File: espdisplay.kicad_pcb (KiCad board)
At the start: 2 copper layers, 34.3 x 30 mm, 11 parts, among them J1 PWR, J2 UReg, J3 DOut, J4 Serial, J5 IO32, SW1 RESET, SW2 BOOT, U1 ESP-WROOM-32

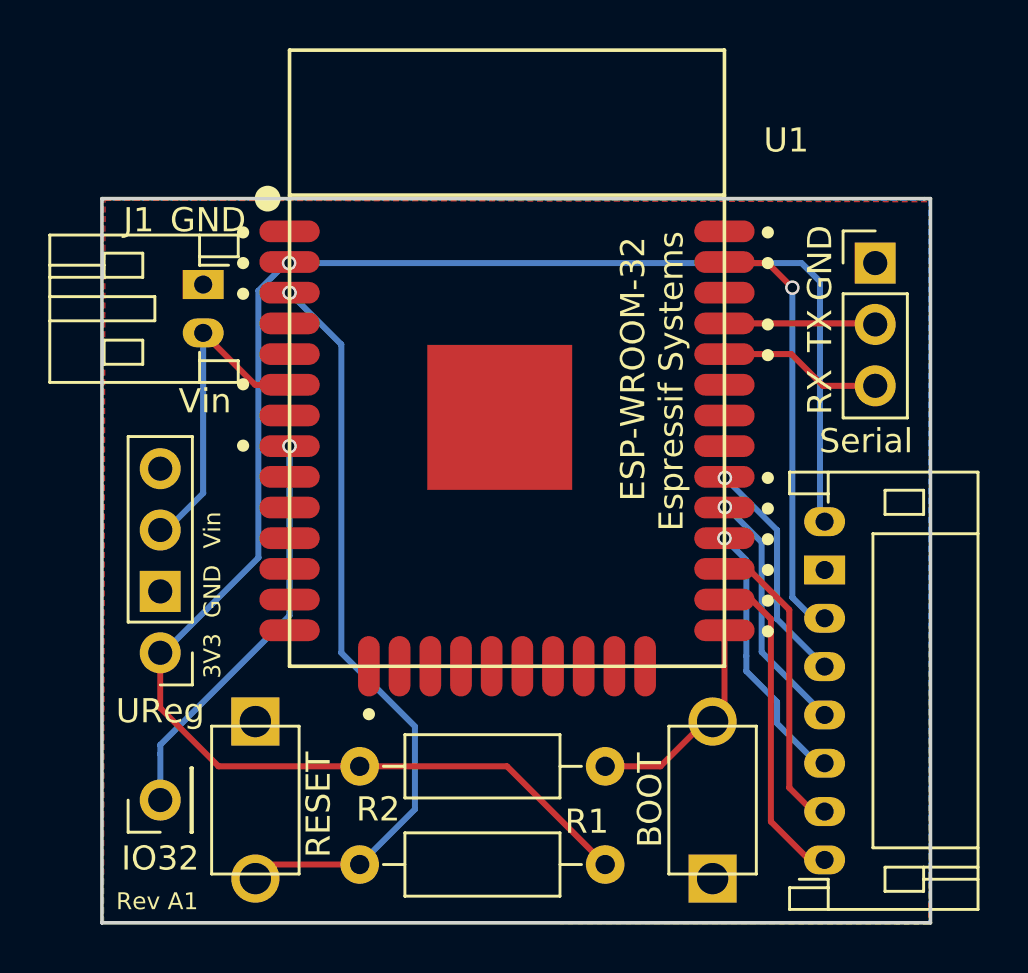
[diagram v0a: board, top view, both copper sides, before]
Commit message: Vias 0.65mm
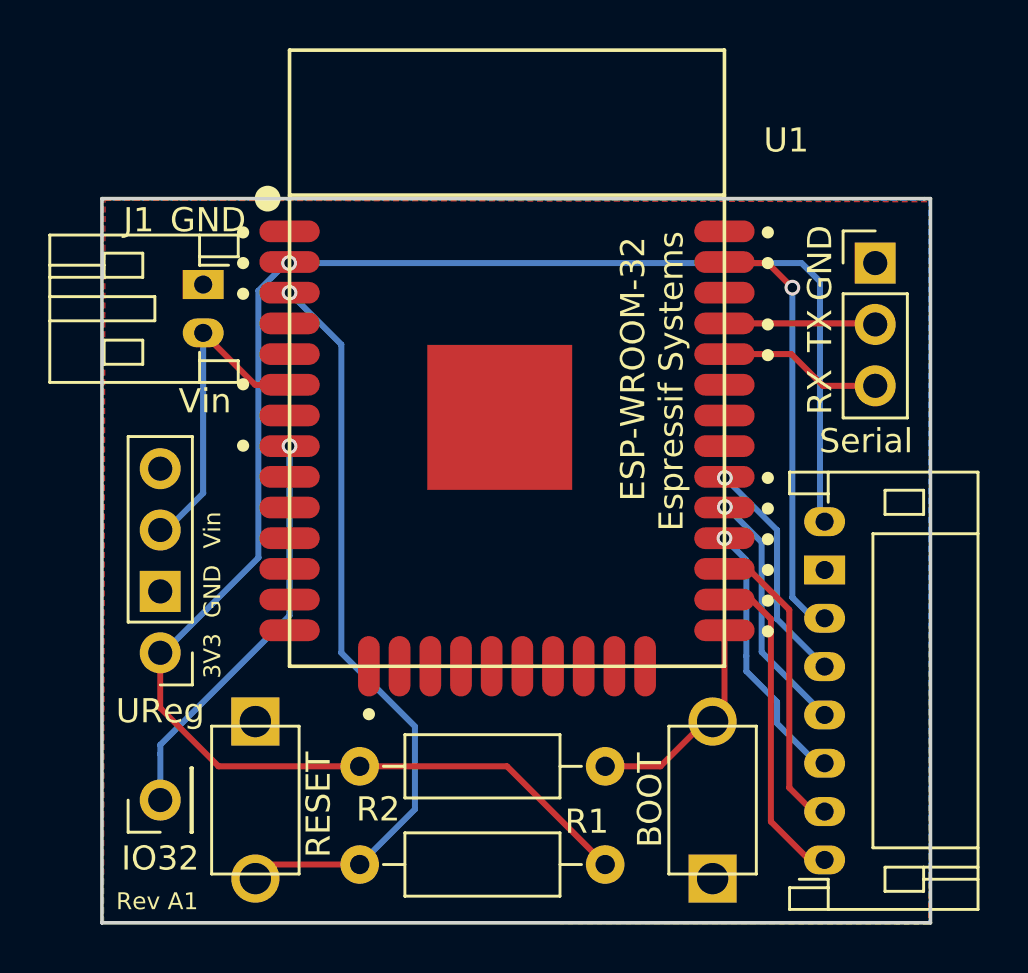
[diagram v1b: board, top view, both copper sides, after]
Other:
- net class Default: via_dia 0.6 -> 0.65
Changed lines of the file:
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@@
     (segment_width 0.25)
     (edge_width 0.15)
-    (via_size 0.6)
+    (via_size 0.65)
     (via_drill 0.4)
     (via_min_size 0.6)
@@
     (clearance 0.2)
     (trace_width 0.25)
-    (via_dia 0.6)
+    (via_dia 0.65)
     (via_drill 0.4)
     (uvia_dia 0.3)
@@
   (segment (start 177.3465 105.263) (end 177.537 105.4535) (width 0.25) (layer B.Cu) (net 3) (status 30))
   (segment (start 155.3755 94.752) (end 155.3925 94.735) (width 0.25) (layer F.Cu) (net 3) (status 30))
-  (via (at 155.3755 94.752) (size 0.6) (drill 0.4) (layers F.Cu B.Cu) (net 3) (status 30))
+  (via (at 155.3755 94.752) (size 0.65) (drill 0.4) (layers F.Cu B.Cu) (net 3) (status 30))
   (segment (start 155.3925 94.735) (end 155.3925 94.709) (width 0.25) (layer F.Cu) (net 3) (status 30))
   (segment (start 155.5025 94.625) (end 155.3925 94.709) (width 0.25) (layer F.Cu) (net 3) (status 80030))
@@
   (segment (start 175.1875 94.752) (end 173.4355 94.752) (width 0.25) (layer F.Cu) (net 4))
   (segment (start 177.062 109.4535) (end 176.2035 108.595) (width 0.25) (layer B.Cu) (net 4))
-  (via (at 176.2035 95.768) (size 0.6) (drill 0.4) (layers F.Cu B.Cu) (net 4))
+  (via (at 176.2035 95.768) (size 0.65) (drill 0.4) (layers F.Cu B.Cu) (net 4))
   (segment (start 176.2035 108.595) (end 176.2035 95.768) (width 0.25) (layer B.Cu) (net 4))
   (segment (start 177.537 109.4535) (end 177.062 109.4535) (width 0.25) (layer B.Cu) (net 4))
   (segment (start 173.3925 103.599) (end 173.3925 103.625) (width 0.25) (layer F.Cu) (net 5) (status 30))
   (segment (start 173.3925 103.625) (end 173.4095 103.642) (width 0.25) (layer F.Cu) (net 5) (status 30))
-  (via (at 173.4095 103.642) (size 0.6) (drill 0.4) (layers F.Cu B.Cu) (net 5) (status 30))
+  (via (at 173.4095 103.642) (size 0.65) (drill 0.4) (layers F.Cu B.Cu) (net 5) (status 30))
   (segment (start 173.4095 103.642) (end 175.5685 105.801) (width 0.25) (layer B.Cu) (net 5))
   (segment (start 175.5685 105.801) (end 175.5685 109.485) (width 0.25) (layer B.Cu) (net 5))
@@
   (segment (start 174.9335 106.309) (end 174.9335 110.85) (width 0.25) (layer B.Cu) (net 6))
   (segment (start 173.3925 104.8655) (end 173.4095 104.8485) (width 0.25) (layer F.Cu) (net 6) (status 30))
-  (via (at 173.4095 104.8485) (size 0.6) (drill 0.4) (layers F.Cu B.Cu) (net 6) (status 30))
+  (via (at 173.4095 104.8485) (size 0.65) (drill 0.4) (layers F.Cu B.Cu) (net 6) (status 30))
   (segment (start 173.3925 104.869) (end 173.3925 104.8655) (width 0.25) (layer F.Cu) (net 6) (status 30))
   (segment (start 177.537 115.4535) (end 177.22 115.4535) (width 0.25) (layer B.Cu) (net 7))
@@
   (segment (start 174.2985 111.643) (end 175.5685 112.913) (width 0.25) (layer B.Cu) (net 7))
   (segment (start 174.2985 111.008) (end 174.2985 111.643) (width 0.25) (layer B.Cu) (net 7))
-  (via (at 173.3925 106.139) (size 0.6) (drill 0.4) (layers F.Cu B.Cu) (net 7))
+  (via (at 173.3925 106.139) (size 0.65) (drill 0.4) (layers F.Cu B.Cu) (net 7))
   (segment (start 174.2985 107.045) (end 174.2985 111.008) (width 0.25) (layer B.Cu) (net 7))
   (segment (start 174.2985 107.045) (end 173.3925 106.139) (width 0.25) (layer B.Cu) (net 7))
@@
   (segment (start 160.5825 117.358) (end 158.2965 119.644) (width 0.25) (layer B.Cu) (net 10) (status 20))
   (segment (start 160.5825 113.929) (end 160.5825 117.358) (width 0.25) (layer B.Cu) (net 10))
-  (via (at 155.3925 95.979) (size 0.6) (drill 0.4) (layers F.Cu B.Cu) (net 10) (status 30))
+  (via (at 155.3925 95.979) (size 0.65) (drill 0.4) (layers F.Cu B.Cu) (net 10) (status 30))
   (segment (start 155.3925 95.979) (end 157.5345 98.121) (width 0.25) (layer B.Cu) (net 10))
   (segment (start 157.5345 98.121) (end 157.5345 110.881) (width 0.25) (layer B.Cu) (net 10))
@@
   (segment (start 150.0415 114.691) (end 150.0415 115.072) (width 0.25) (layer B.Cu) (net 37))
   (segment (start 150.0415 115.072) (end 150.0415 116.977) (width 0.25) (layer B.Cu) (net 37))
-  (via (at 155.3925 102.329) (size 0.6) (drill 0.4) (layers F.Cu B.Cu) (net 37))
+  (via (at 155.3925 102.329) (size 0.65) (drill 0.4) (layers F.Cu B.Cu) (net 37))
   (zone (net 2) (net_name GND) (layer F.Cu) (hatch edge 0.508)
     (connect_pads (clearance 0.508))

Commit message: Trace width
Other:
- net class PWR added: clearance 0.2, trace_width 0.6, via_dia 0.8, via_drill 0.4
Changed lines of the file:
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@@
     (links 28)
     (no_connects 0)
-    (area 143.5945 83.49 185.862 122.132001)
+    (area 147.553499 92.009999 181.993501 122.132001)
     (thickness 1.6)
     (drawings 38)
-    (tracks 89)
+    (tracks 79)
     (zones 0)
     (modules 11)
@@
     (uvia_dia 0.3)
     (uvia_drill 0.1)
-    (add_net +3V3)
     (add_net /BUSY)
     (add_net /CLK)
@@
     (add_net /IO32)
     (add_net /RST)
-    (add_net /Vin)
-    (add_net GND)
     (add_net "Net-(J2-Pad4)")
     (add_net "Net-(J4-Pad2)")
@@
     (add_net "Net-(U1-Pad7)")
     (add_net "Net-(U1-Pad9)")
+  )
+  (net_class PWR ""
+    (clearance 0.2)
+    (trace_width 0.6)
+    (via_dia 0.8)
+    (via_drill 0.4)
+    (uvia_dia 0.3)
+    (uvia_drill 0.1)
+    (add_net +3V3)
+    (add_net /Vin)
+    (add_net GND)
   )
   (module Symbols:OSHW-Logo_7.5x8mm_SilkScreen (layer B.Cu)
@@
   )
   (segment (start 150.0415 105.801) (end 150.2955 105.801) (width 0.25) (layer B.Cu) (net 1))
-  (segment (start 150.2955 105.801) (end 151.8195 104.277) (width 0.25) (layer B.Cu) (net 1))
-  (segment (start 151.8195 97.641) (end 151.8195 104.277) (width 0.25) (layer B.Cu) (net 1) (status 10))
-  (segment (start 155.3925 99.789) (end 153.9675 99.789) (width 0.25) (layer F.Cu) (net 1) (status 10))
-  (segment (start 153.9675 99.789) (end 151.8195 97.641) (width 0.25) (layer F.Cu) (net 1) (status 20))
-  (segment (start 155.3755 94.752) (end 155.2485 94.752) (width 0.25) (layer B.Cu) (net 3))
-  (segment (start 155.2485 94.752) (end 154.1055 95.895) (width 0.25) (layer B.Cu) (net 3))
+  (segment (start 150.2955 105.801) (end 151.8195 104.277) (width 0.6) (layer B.Cu) (net 1))
+  (segment (start 151.8195 97.641) (end 151.8195 104.277) (width 0.6) (layer B.Cu) (net 1) (status 10))
+  (segment (start 155.3925 99.789) (end 153.9675 99.789) (width 0.6) (layer F.Cu) (net 1) (status 10))
+  (segment (start 153.9675 99.789) (end 151.8195 97.641) (width 0.6) (layer F.Cu) (net 1) (status 20))
+  (segment (start 155.3755 94.752) (end 154.294924 95.832576) (width 0.6) (layer B.Cu) (net 3))
+  (segment (start 154.294924 95.832576) (end 154.294924 106.754576) (width 0.6) (layer B.Cu) (net 3))
+  (segment (start 154.294924 106.754576) (end 150.1685 110.881) (width 0.6) (layer B.Cu) (net 3))
   (segment (start 150.0415 110.881) (end 150.1685 110.881) (width 0.25) (layer B.Cu) (net 3))
-  (segment (start 150.1685 110.881) (end 154.1055 106.944) (width 0.25) (layer B.Cu) (net 3))
-  (segment (start 154.1055 95.895) (end 154.1055 106.944) (width 0.25) (layer B.Cu) (net 3))
-  (segment (start 177.3465 95.514) (end 176.5845 94.752) (width 0.25) (layer B.Cu) (net 3))
-  (segment (start 177.3465 95.514) (end 177.3465 105.263) (width 0.25) (layer B.Cu) (net 3))
-  (segment (start 158.2965 115.58) (end 152.4545 115.58) (width 0.25) (layer F.Cu) (net 3) (status 10))
-  (segment (start 150.0415 113.167) (end 150.0415 110.881) (width 0.25) (layer F.Cu) (net 3))
-  (segment (start 152.4545 115.58) (end 150.0415 113.167) (width 0.25) (layer F.Cu) (net 3))
-  (segment (start 158.2965 115.58) (end 164.3925 115.58) (width 0.25) (layer F.Cu) (net 3) (status 10))
-  (segment (start 164.3925 115.58) (end 168.4565 119.644) (width 0.25) (layer F.Cu) (net 3))
-  (segment (start 155.3755 94.752) (end 176.5845 94.752) (width 0.25) (layer B.Cu) (net 3))
+  (segment (start 177.3465 95.514) (end 176.5845 94.752) (width 0.6) (layer B.Cu) (net 3))
+  (segment (start 177.3465 95.514) (end 177.3465 105.263) (width 0.6) (layer B.Cu) (net 3))
+  (segment (start 158.2965 115.58) (end 152.4545 115.58) (width 0.6) (layer F.Cu) (net 3) (status 10))
+  (segment (start 150.0415 113.167) (end 150.0415 110.881) (width 0.6) (layer F.Cu) (net 3))
+  (segment (start 152.4545 115.58) (end 150.0415 113.167) (width 0.6) (layer F.Cu) (net 3))
+  (segment (start 158.2965 115.58) (end 164.3925 115.58) (width 0.6) (layer F.Cu) (net 3) (status 10))
+  (segment (start 164.3925 115.58) (end 168.4565 119.644) (width 0.6) (layer F.Cu) (net 3))
+  (segment (start 155.3755 94.752) (end 176.5845 94.752) (width 0.6) (layer B.Cu) (net 3))
   (segment (start 177.3465 105.263) (end 177.537 105.4535) (width 0.25) (layer B.Cu) (net 3) (status 30))
-  (segment (start 155.3755 94.752) (end 155.3925 94.735) (width 0.25) (layer F.Cu) (net 3) (status 30))
-  (via (at 155.3755 94.752) (size 0.65) (drill 0.4) (layers F.Cu B.Cu) (net 3) (status 30))
-  (segment (start 155.3925 94.735) (end 155.3925 94.709) (width 0.25) (layer F.Cu) (net 3) (status 30))
-  (segment (start 155.5025 94.625) (end 155.3925 94.709) (width 0.25) (layer F.Cu) (net 3) (status 80030))
+  (via (at 155.3755 94.752) (size 0.8) (drill 0.4) (layers F.Cu B.Cu) (net 3) (status 30))
   (segment (start 176.2035 95.768) (end 175.1875 94.752) (width 0.25) (layer F.Cu) (net 4))
   (segment (start 175.1875 94.752) (end 173.4355 94.752) (width 0.25) (layer F.Cu) (net 4))
@@
   (segment (start 176.2035 108.595) (end 176.2035 95.768) (width 0.25) (layer B.Cu) (net 4))
   (segment (start 177.537 109.4535) (end 177.062 109.4535) (width 0.25) (layer B.Cu) (net 4))
-  (segment (start 173.3925 103.599) (end 173.3925 103.625) (width 0.25) (layer F.Cu) (net 5) (status 30))
-  (segment (start 173.3925 103.625) (end 173.4095 103.642) (width 0.25) (layer F.Cu) (net 5) (status 30))
   (via (at 173.4095 103.642) (size 0.65) (drill 0.4) (layers F.Cu B.Cu) (net 5) (status 30))
   (segment (start 173.4095 103.642) (end 175.5685 105.801) (width 0.25) (layer B.Cu) (net 5))
   (segment (start 175.5685 105.801) (end 175.5685 109.485) (width 0.25) (layer B.Cu) (net 5))
   (segment (start 175.5685 109.485) (end 177.537 111.4535) (width 0.25) (layer B.Cu) (net 5) (status 20))
-  (segment (start 173.4095 104.8485) (end 173.473 104.8485) (width 0.25) (layer B.Cu) (net 6))
   (segment (start 173.473 104.8485) (end 174.9335 106.309) (width 0.25) (layer B.Cu) (net 6))
   (segment (start 174.9335 110.85) (end 177.537 113.4535) (width 0.25) (layer B.Cu) (net 6) (status 20))
   (segment (start 174.9335 106.309) (end 174.9335 110.85) (width 0.25) (layer B.Cu) (net 6))
-  (segment (start 173.3925 104.8655) (end 173.4095 104.8485) (width 0.25) (layer F.Cu) (net 6) (status 30))
   (via (at 173.4095 104.8485) (size 0.65) (drill 0.4) (layers F.Cu B.Cu) (net 6) (status 30))
-  (segment (start 173.3925 104.869) (end 173.3925 104.8655) (width 0.25) (layer F.Cu) (net 6) (status 30))
   (segment (start 177.537 115.4535) (end 177.22 115.4535) (width 0.25) (layer B.Cu) (net 7))
   (segment (start 177.22 115.4535) (end 175.5685 113.802) (width 0.25) (layer B.Cu) (net 7))
@@
   (segment (start 176.1605 98.519) (end 177.4735 99.832) (width 0.25) (layer F.Cu) (net 13))
   (segment (start 177.4735 99.832) (end 179.6325 99.832) (width 0.25) (layer F.Cu) (net 13))
-  (segment (start 155.3925 102.329) (end 155.391104 102.330396) (width 0.25) (layer B.Cu) (net 37))
   (segment (start 155.391104 102.330396) (end 155.391104 109.341396) (width 0.25) (layer B.Cu) (net 37))
   (segment (start 155.391104 109.341396) (end 150.0415 114.691) (width 0.25) (layer B.Cu) (net 37))

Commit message: Trace cleanup
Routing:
- net Net-(R2-Pad2): track 10.2 -> 9.19 mm
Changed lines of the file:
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@@
     (thickness 1.6)
     (drawings 38)
-    (tracks 79)
+    (tracks 73)
     (zones 0)
     (modules 11)
@@
   (segment (start 154.294924 95.832576) (end 154.294924 106.754576) (width 0.6) (layer B.Cu) (net 3))
   (segment (start 154.294924 106.754576) (end 150.1685 110.881) (width 0.6) (layer B.Cu) (net 3))
-  (segment (start 150.0415 110.881) (end 150.1685 110.881) (width 0.25) (layer B.Cu) (net 3))
   (segment (start 177.3465 95.514) (end 176.5845 94.752) (width 0.6) (layer B.Cu) (net 3))
   (segment (start 177.3465 95.514) (end 177.3465 105.263) (width 0.6) (layer B.Cu) (net 3))
@@
   (segment (start 158.2965 119.644) (end 154.5615 119.644) (width 0.25) (layer F.Cu) (net 10))
   (segment (start 154.5615 119.644) (end 153.9785 120.227) (width 0.25) (layer F.Cu) (net 10))
-  (segment (start 158.2965 119.644) (end 158.2965 119.7075) (width 0.25) (layer F.Cu) (net 10))
   (segment (start 160.5825 113.929) (end 157.5345 110.881) (width 0.25) (layer B.Cu) (net 10))
   (segment (start 160.5825 117.358) (end 158.2965 119.644) (width 0.25) (layer B.Cu) (net 10) (status 20))
@@
   (segment (start 155.3925 95.979) (end 157.5345 98.121) (width 0.25) (layer B.Cu) (net 10))
   (segment (start 157.5345 98.121) (end 157.5345 110.881) (width 0.25) (layer B.Cu) (net 10))
-  (segment (start 155.5025 95.895) (end 155.3925 95.979) (width 0.25) (layer F.Cu) (net 10) (status 80030))
   (segment (start 172.9015 113.727) (end 172.5955 113.727) (width 0.25) (layer F.Cu) (net 11) (status 30))
   (segment (start 172.5955 113.727) (end 170.7425 115.58) (width 0.25) (layer F.Cu) (net 11) (status 10))
@@
   (segment (start 173.3925 109.949) (end 173.3925 113.236) (width 0.25) (layer F.Cu) (net 11) (status 20))
   (segment (start 173.3925 113.236) (end 172.9015 113.727) (width 0.25) (layer F.Cu) (net 11) (status 30))
-  (segment (start 168.4565 115.58) (end 169.2185 115.58) (width 0.25) (layer F.Cu) (net 11) (status 30))
-  (segment (start 173.0115 113.617) (end 172.9015 113.727) (width 0.25) (layer F.Cu) (net 11) (status 30))
-  (segment (start 172.9015 113.727) (end 172.9015 113.675) (width 0.25) (layer F.Cu) (net 11) (status 80030))
   (segment (start 173.3925 97.249) (end 179.5895 97.249) (width 0.25) (layer F.Cu) (net 12) (status 30))
   (segment (start 179.5895 97.249) (end 179.6325 97.292) (width 0.25) (layer F.Cu) (net 12) (status 30))

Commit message: "merge" rev.a2
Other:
- rule via_min_size: 0.6 -> 0.65
- board text added: "Rev A2"
- board text removed: "Rev A1"
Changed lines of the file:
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@@
     (links 28)
     (no_connects 0)
-    (area 147.553499 92.009999 181.993501 122.132001)
+    (area 143.5945 83.49 185.862 122.132001)
     (thickness 1.6)
     (drawings 38)
-    (tracks 73)
+    (tracks 74)
     (zones 0)
     (modules 11)
@@
     (via_size 0.65)
     (via_drill 0.4)
-    (via_min_size 0.6)
+    (via_min_size 0.65)
     (via_min_drill 0.4)
     (uvia_size 0.3)
@@
     (descr "JST PH series connector, S2B-PH-K, side entry type, through hole, Datasheet: http://www.jst-mfg.com/product/pdf/eng/ePH.pdf")
     (tags "connector jst ph")
-    (fp_text reference J1 (at -2.667 2.667 360) (layer F.SilkS)
+    (fp_text reference J1 (at -2.5908 2.667 360) (layer F.SilkS)
       (effects (font (size 1 1) (thickness 0.15)))
     )
@@
     (effects (font (size 0.7 0.7) (thickness 0.15)) (justify mirror))
   )
-  (gr_text GND (at 152.0195 92.9735) (layer F.SilkS)
+  (gr_text GND (at 152.0195 93.0497) (layer F.SilkS)
     (effects (font (size 1 1) (thickness 0.15)))
   )
-  (gr_text "Rev A1" (at 149.9145 121.168) (layer F.SilkS)
+  (gr_text "Rev A2" (at 149.9145 121.168) (layer F.SilkS)
     (effects (font (size 0.7 0.7) (thickness 0.12)))
   )
@@
   (segment (start 155.3925 99.789) (end 153.9675 99.789) (width 0.6) (layer F.Cu) (net 1) (status 10))
   (segment (start 153.9675 99.789) (end 151.8195 97.641) (width 0.6) (layer F.Cu) (net 1) (status 20))
-  (segment (start 155.3755 94.752) (end 154.294924 95.832576) (width 0.6) (layer B.Cu) (net 3))
-  (segment (start 154.294924 95.832576) (end 154.294924 106.754576) (width 0.6) (layer B.Cu) (net 3))
+  (segment (start 177.3465 105.263) (end 177.3465 95.405149) (width 0.6) (layer B.Cu) (net 3))
+  (segment (start 177.3465 95.405149) (end 176.693351 94.752) (width 0.6) (layer B.Cu) (net 3))
+  (segment (start 176.693351 94.752) (end 155.3755 94.752) (width 0.6) (layer B.Cu) (net 3))
+  (segment (start 155.3755 94.752) (end 154.733344 94.752) (width 0.6) (layer B.Cu) (net 3))
+  (segment (start 154.733344 94.752) (end 154.294924 95.19042) (width 0.6) (layer B.Cu) (net 3))
+  (segment (start 154.294924 95.19042) (end 154.294924 106.754576) (width 0.6) (layer B.Cu) (net 3))
   (segment (start 154.294924 106.754576) (end 150.1685 110.881) (width 0.6) (layer B.Cu) (net 3))
-  (segment (start 177.3465 95.514) (end 176.5845 94.752) (width 0.6) (layer B.Cu) (net 3))
-  (segment (start 177.3465 95.514) (end 177.3465 105.263) (width 0.6) (layer B.Cu) (net 3))
   (segment (start 158.2965 115.58) (end 152.4545 115.58) (width 0.6) (layer F.Cu) (net 3) (status 10))
   (segment (start 150.0415 113.167) (end 150.0415 110.881) (width 0.6) (layer F.Cu) (net 3))
@@
   (segment (start 158.2965 115.58) (end 164.3925 115.58) (width 0.6) (layer F.Cu) (net 3) (status 10))
   (segment (start 164.3925 115.58) (end 168.4565 119.644) (width 0.6) (layer F.Cu) (net 3))
-  (segment (start 155.3755 94.752) (end 176.5845 94.752) (width 0.6) (layer B.Cu) (net 3))
   (segment (start 177.3465 105.263) (end 177.537 105.4535) (width 0.25) (layer B.Cu) (net 3) (status 30))
   (via (at 155.3755 94.752) (size 0.8) (drill 0.4) (layers F.Cu B.Cu) (net 3) (status 30))
